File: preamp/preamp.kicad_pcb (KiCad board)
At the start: 2 copper layers, 21 parts, among them P101 CONN_01X02, P102 USB_OTG, U101 CONN_SMA, U102 HMC476MP86, U103 CONN_SMA

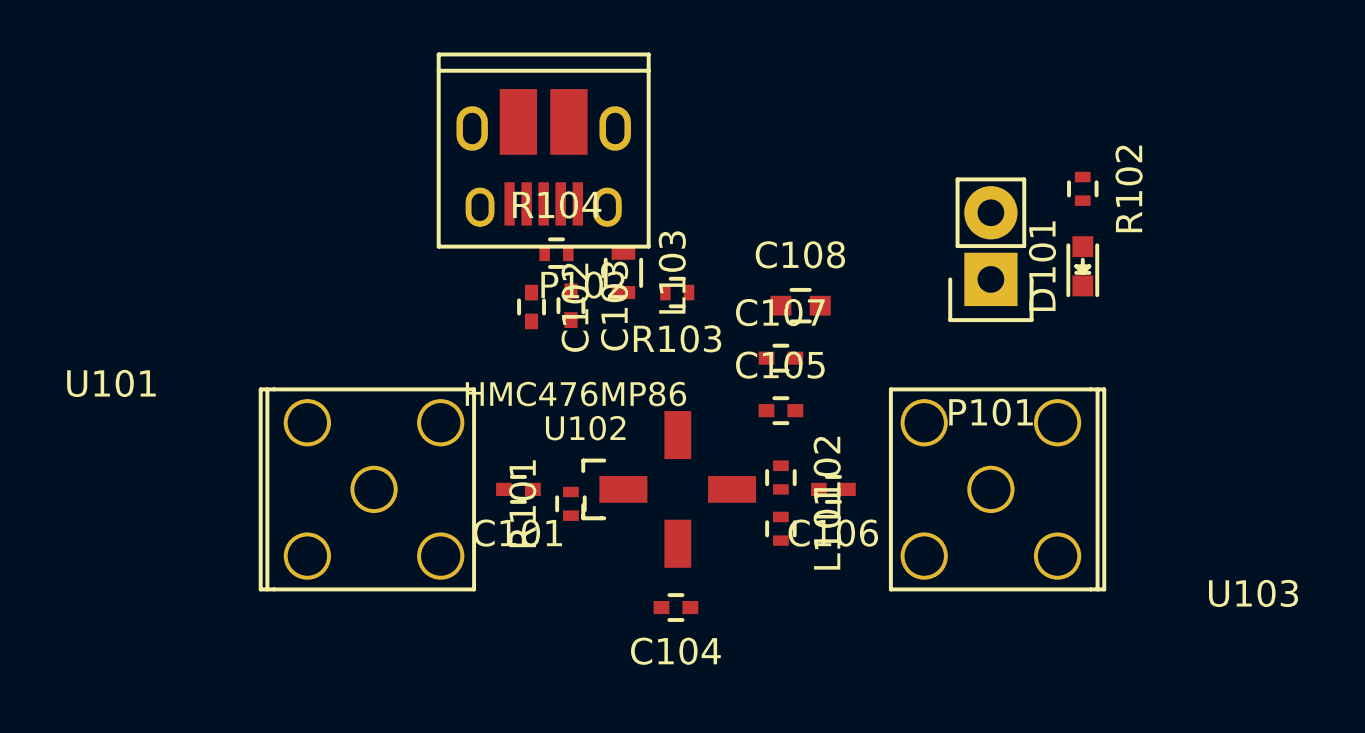
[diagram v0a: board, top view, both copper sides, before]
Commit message: added layout for preamp
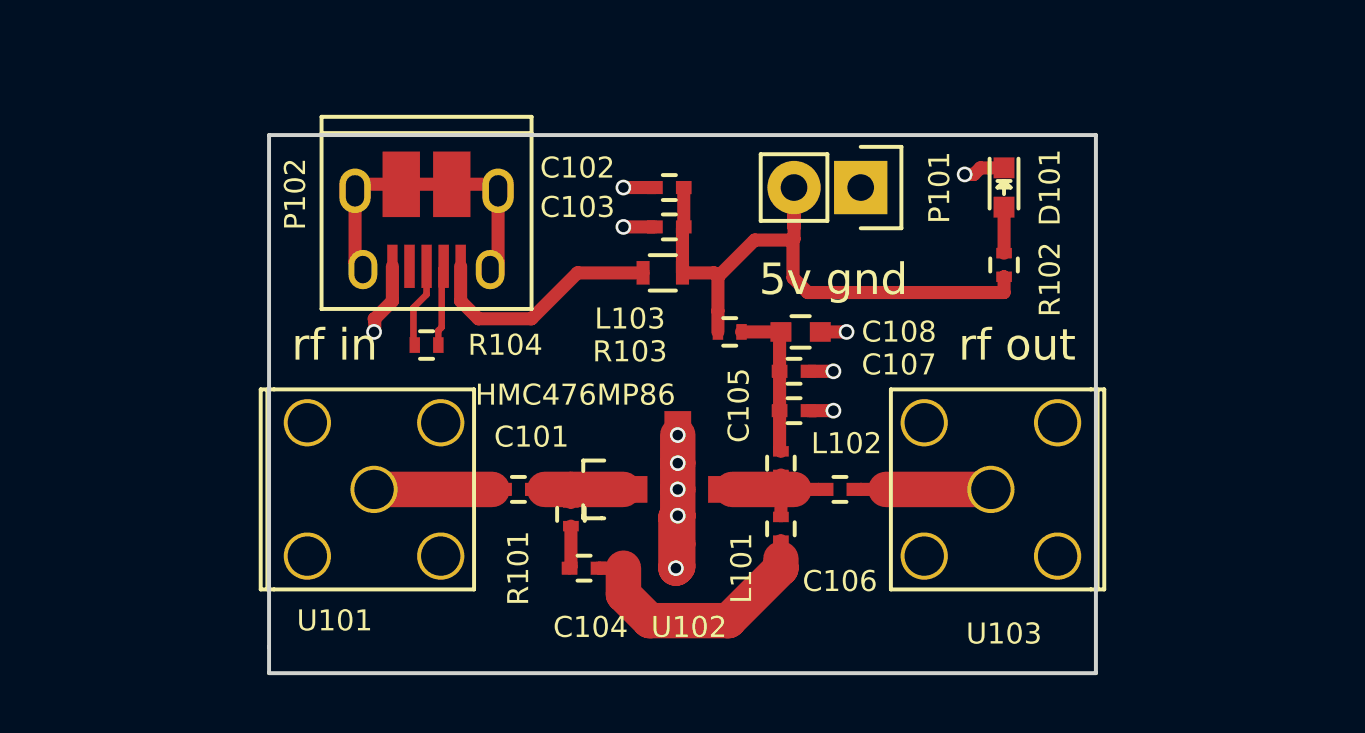
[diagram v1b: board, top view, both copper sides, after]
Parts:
- moved C102 6.95 mm to (113.8, 73.5), turned to 180 degrees
- moved P101 6.07 mm to (121.0, 73.5), turned to 270 degrees
- moved R104 6.06 mm to (104.5, 79.5)
- moved P102 5.06 mm to (104.5, 75.0)
- moved C103 4.80 mm to (113.8, 75.0), turned to 180 degrees
- moved D101 4.24 mm to (126.5, 73.5), turned to 270 degrees
- moved R102 4.17 mm to (126.5, 76.5), turned to 90 degrees
- moved C104 3.81 mm to (110.5, 88.0)
- moved R103 2.50 mm to (116.0, 79.0)
- moved L103 1.50 mm to (113.5, 76.8), turned to 0 degrees
- moved C108 1.00 mm to (118.8, 79.0)
- moved C107 0.71 mm to (118.5, 80.5)
- moved L102 0.55 mm to (118.0, 84.0)
- moved C105 0.50 mm to (118.5, 82.0)
- moved R101 0.40 mm to (110.0, 86.0)
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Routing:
- net Net-(C102-Pad1): track 0.00 -> 23.6 mm
- net GND: track 0.00 -> 16.8 mm, vias 0 -> 12
- net Net-(P102-Pad6): track 0.00 -> 11.9 mm
- net Net-(C104-Pad1): track 0.00 -> 10.2 mm
- net Net-(L103-Pad1): track 0.00 -> 9.28 mm
- net Net-(C105-Pad1): track 0.00 -> 6.09 mm
- net Net-(C106-Pad2): track 0.00 -> 5.36 mm
- net Net-(C106-Pad1): track 0.00 -> 5.00 mm
- net Net-(C101-Pad2): track 0.00 -> 4.95 mm
- net Net-(C101-Pad1): track 0.00 -> 4.95 mm
- net Net-(P102-Pad3): track 0.00 -> 3.23 mm
- net Net-(P102-Pad2): track 0.00 -> 3.08 mm
- net Net-(D101-Pad2): track 0.00 -> 1.75 mm
- net Net-(C104-Pad2): track 0.00 -> 1.62 mm
- added copper zone on B.Cu, net GND
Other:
- board outline added: 31.5 x 20.5 mm
- net class Default: clearance 0.2 -> 0.127
- rule trace_clearance: 0.2 -> 0.127
- rule trace_min: 0.2 -> 0.127
- board text added: "5v gnd"
- board text added: "rf in"
- board text added: "rf out"
